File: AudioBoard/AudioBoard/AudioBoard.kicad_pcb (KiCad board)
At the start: 4 copper layers, 250 x 160 mm, 211 parts, among them U5 TL072, U6 TL072, U7 TL072, U8 TL072, U9 TL072

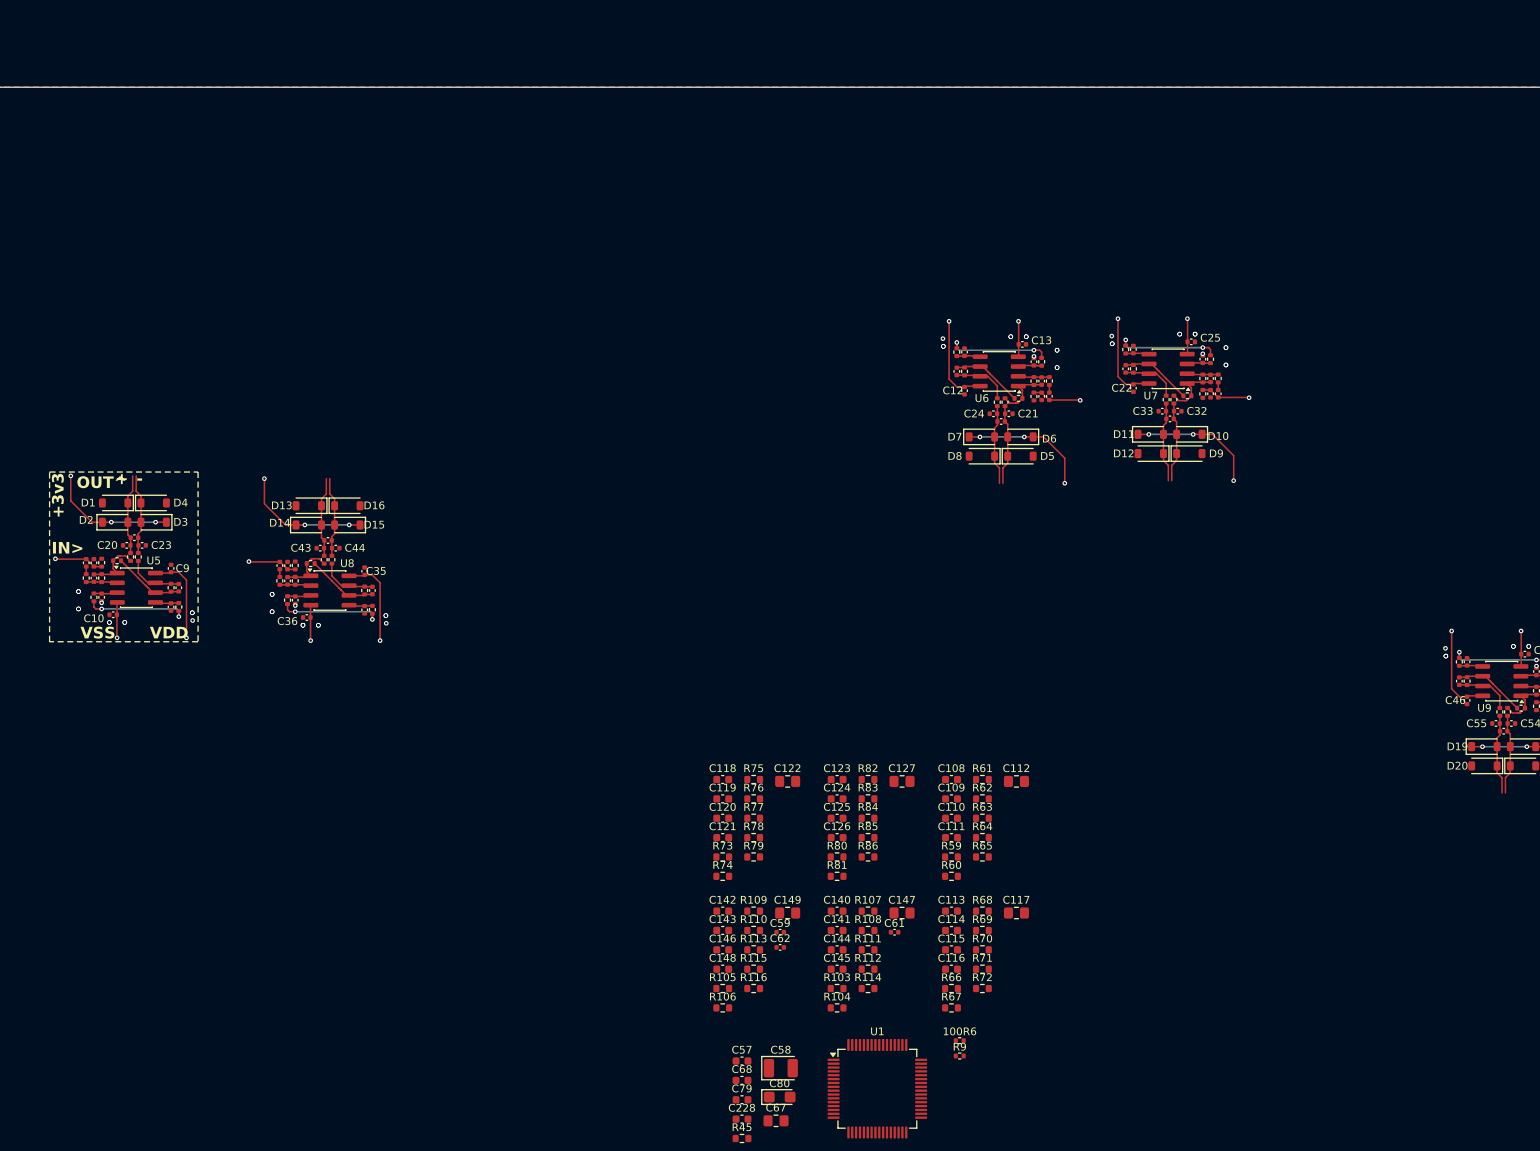
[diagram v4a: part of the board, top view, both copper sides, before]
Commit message: added jack IO, headphone amp cirucit
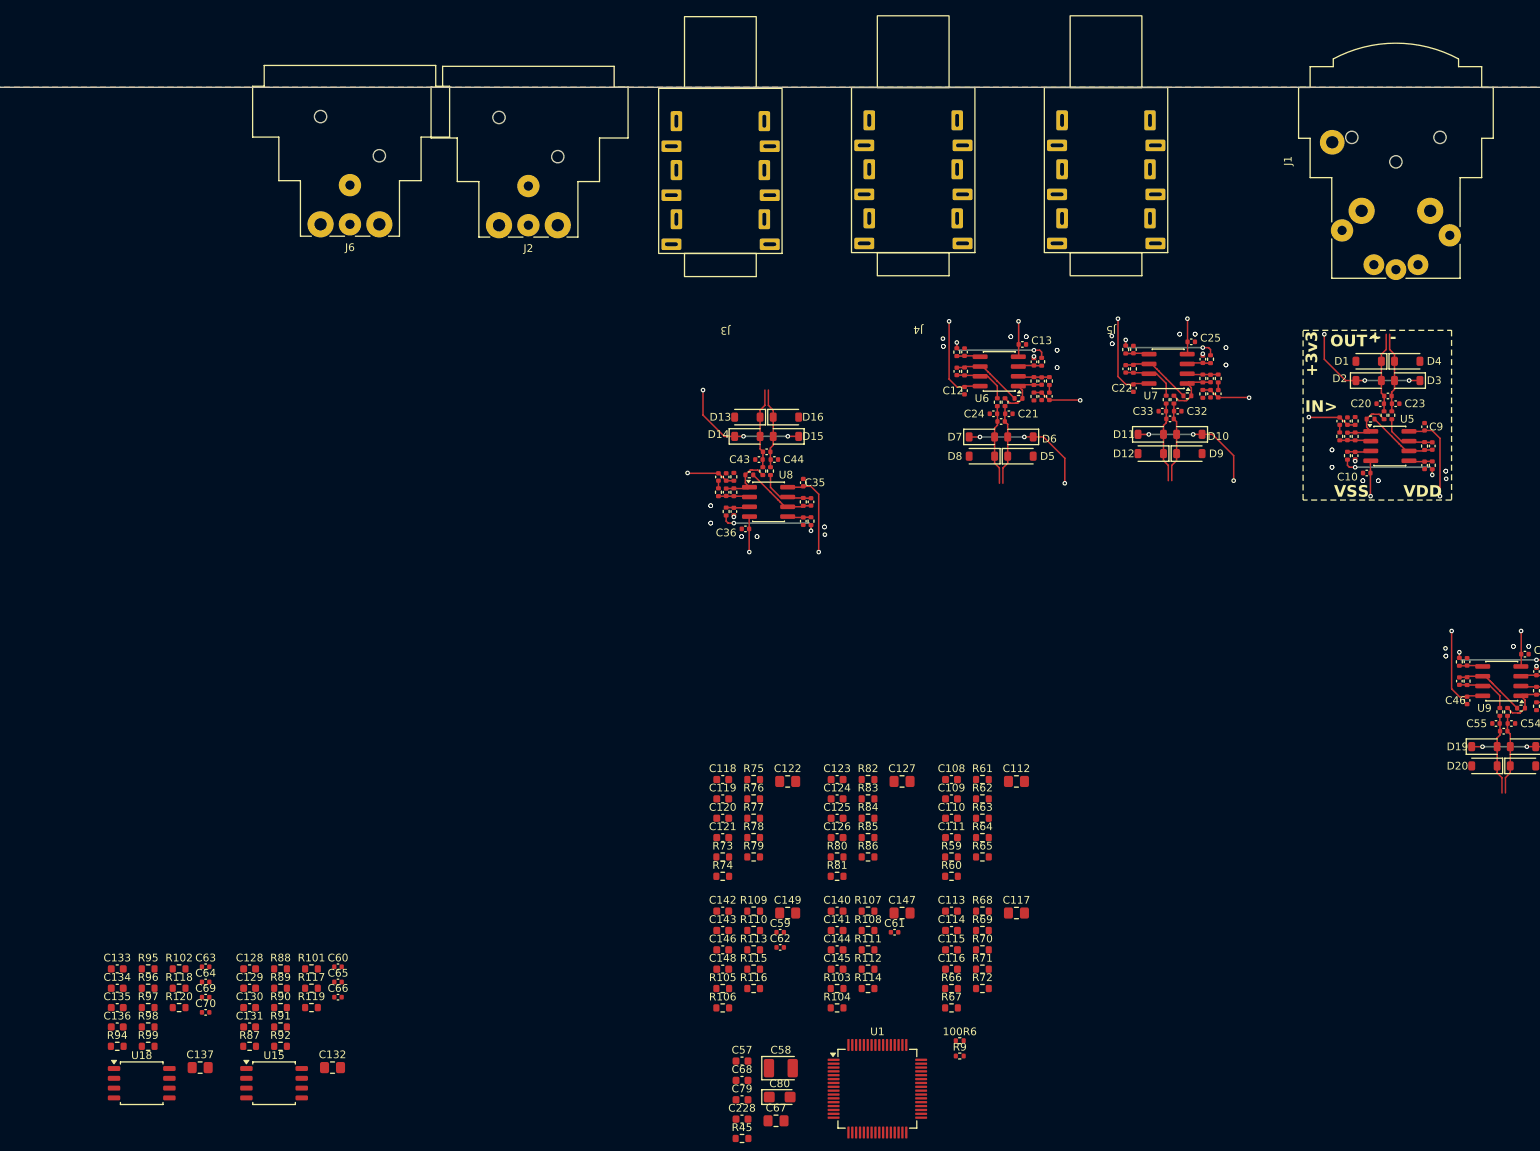
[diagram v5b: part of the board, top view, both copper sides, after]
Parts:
- added C128: 470pF, Capacitor_SMD:C_0603_1608Metric, F.Cu at (116.7, 174.3)
- added C129: 470pF, Capacitor_SMD:C_0603_1608Metric, F.Cu at (116.7, 176.8)
- added C130: 100pF, Capacitor_SMD:C_0603_1608Metric, F.Cu at (116.7, 179.3)
- added C131: 100pF, Capacitor_SMD:C_0603_1608Metric, F.Cu at (116.7, 181.8)
- added C132: 2.2uF, Capacitor_SMD:C_0805_2012Metric_Pad1.18x1.45mm_HandSolder, F.Cu at (127.4, 187.1)
- added C133: 470pF, Capacitor_SMD:C_0603_1608Metric, F.Cu at (99.5, 174.3)
- added C134: 470pF, Capacitor_SMD:C_0603_1608Metric, F.Cu at (99.5, 176.8)
- added C135: 100pF, Capacitor_SMD:C_0603_1608Metric, F.Cu at (99.5, 179.3)
- added C136: 100pF, Capacitor_SMD:C_0603_1608Metric, F.Cu at (99.5, 181.8)
- added C137: 2.2uF, Capacitor_SMD:C_0805_2012Metric_Pad1.18x1.45mm_HandSolder, F.Cu at (110.3, 187.1)
- added C60: 100n, Capacitor_SMD:C_0402_1005Metric, F.Cu at (128.1, 174.0)
- added C63: 100n, Capacitor_SMD:C_0402_1005Metric, F.Cu at (111.0, 174.0)
- added C64: 100n, Capacitor_SMD:C_0402_1005Metric, F.Cu at (111.0, 176.0)
- added C65: 100n, Capacitor_SMD:C_0402_1005Metric, F.Cu at (128.1, 176.0)
- added C66: 100n, Capacitor_SMD:C_0402_1005Metric, F.Cu at (128.1, 178.0)
- added C69: 100n, Capacitor_SMD:C_0402_1005Metric, F.Cu at (111.0, 178.0)
- added C70: 100n, Capacitor_SMD:C_0402_1005Metric, F.Cu at (111.0, 179.9)
- added J1: IN, Connector_Audio:Jack_XLR-6.35mm_Neutrik_NCJ6FA-H_Horizontal, F.Cu at (258.3, 78.6)
- added J2: XLR_L, Connector_Audio:Jack_XLR_Neutrik_NC3MAH_Horizontal, F.Cu at (156.6, 77.9)
- added J3: FX_RETURN, haoyu:HAOYU_PJ-625, F.Cu at (182.4, 84.5)
- added J4: FX_SEND, haoyu:HAOYU_PJ-625, F.Cu at (207.4, 84.4)
- added J5: INS_OUT, haoyu:HAOYU_PJ-625, F.Cu at (232.3, 84.4)
- added J6: XLR_R, Connector_Audio:Jack_XLR_Neutrik_NC3MAH_Horizontal, F.Cu at (133.5, 77.8)
- added R101: 40k, Resistor_SMD:R_0603_1608Metric, F.Cu at (124.7, 174.3)
- added R102: 40k, Resistor_SMD:R_0603_1608Metric, F.Cu at (107.5, 174.3)
- added R117: 1R, Resistor_SMD:R_0603_1608Metric, F.Cu at (124.7, 176.8)
- added R118: 1R, Resistor_SMD:R_0603_1608Metric, F.Cu at (107.5, 176.8)
- added R119: 1R, Resistor_SMD:R_0603_1608Metric, F.Cu at (124.7, 179.3)
- added R120: 1R, Resistor_SMD:R_0603_1608Metric, F.Cu at (107.5, 179.3)
- added R87: 3k, Resistor_SMD:R_0603_1608Metric, F.Cu at (116.7, 184.3)
- added R88: 3k, Resistor_SMD:R_0603_1608Metric, F.Cu at (120.7, 174.3)
- added R89: 3k, Resistor_SMD:R_0603_1608Metric, F.Cu at (120.7, 176.8)
- added R90: 3k, Resistor_SMD:R_0603_1608Metric, F.Cu at (120.7, 179.3)
- added R91: 3k, Resistor_SMD:R_0603_1608Metric, F.Cu at (120.7, 181.8)
- added R92: 3k, Resistor_SMD:R_0603_1608Metric, F.Cu at (120.7, 184.3)
- added R94: 3k, Resistor_SMD:R_0603_1608Metric, F.Cu at (99.5, 184.3)
- added R95: 3k, Resistor_SMD:R_0603_1608Metric, F.Cu at (103.5, 174.3)
- added R96: 3k, Resistor_SMD:R_0603_1608Metric, F.Cu at (103.5, 176.8)
- added R97: 3k, Resistor_SMD:R_0603_1608Metric, F.Cu at (103.5, 179.3)
- added R98: 3k, Resistor_SMD:R_0603_1608Metric, F.Cu at (103.5, 181.8)
- added R99: 3k, Resistor_SMD:R_0603_1608Metric, F.Cu at (103.5, 184.3)
- added U15: NJM4556A, Package_SO:SOIC-8_5.3x5.3mm_P1.27mm, F.Cu at (119.8, 189.1)
- added U18: NJM4556A, Package_SO:SOIC-8_5.3x5.3mm_P1.27mm, F.Cu at (102.7, 189.1)
- C55: value 1n -> 100n
- moved 100R1 163.6 mm to (270.0, 109.0)
- moved C10 163.6 mm to (261.5, 110.0)
- moved C11 163.6 mm to (259.0, 105.3)
- moved C14 163.6 mm to (270.0, 106.5)
- moved C17 163.6 mm to (269.0, 109.0)
- moved C2 163.6 mm to (259.0, 103.3)
- moved C20 163.6 mm to (263.2, 101.0)
- moved C23 163.6 mm to (265.2, 101.0)
- moved C26 163.6 mm to (264.2, 100.0)
- moved C5 163.6 mm to (258.0, 103.3)
- moved C8 163.6 mm to (260.0, 107.8)
- moved C9 163.6 mm to (269.0, 104.0)
- moved D1 163.6 mm to (261.8, 98.0)
- moved D2 163.6 mm to (261.8, 95.5)
- moved D3 163.6 mm to (266.8, 98.0)
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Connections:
- net /MIC_preamp/IN_N renamed /Audio_IO_conn/xlr_in_n
- net /MIC_preamp/IN_P renamed /Audio_IO_conn/xlr_in_p
- C55 pad 1: /Instrument_Input5/OUT_N -> /HeadphoneAmplifier/VDD
- R4 pad 1: /Instrument_Input/IN -> /Audio_IO_conn/ins_in
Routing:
- net (no net): track 26.1 -> 14.1 mm, vias 3 -> 2
- net VDD: track 48.0 -> 60.0 mm, vias 4 -> 5

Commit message: added connectors to pcb
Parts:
- added J7: Barrel_Jack, Connector_BarrelJack:BarrelJack_Wuerth_6941xx301002, F.Cu at (59.5, 74.0)
- added J8: NMJ6HFD2, Connector_Audio:Jack_6.35mm_Neutrik_NMJ6HFD2_Horizontal, F.Cu at (89.3, 76.8)
- added J9: NMJ6HFD2, Connector_Audio:Jack_6.35mm_Neutrik_NMJ6HFD2_Horizontal, F.Cu at (282.0, 77.0)
- added SW2: SW_SPDT_321, haoyu:SS-12D28G7, F.Cu at (70.0, 84.6)
- added SW3: PWR_SW, haoyu:SS-12D28G7, F.Cu at (111.0, 84.6)

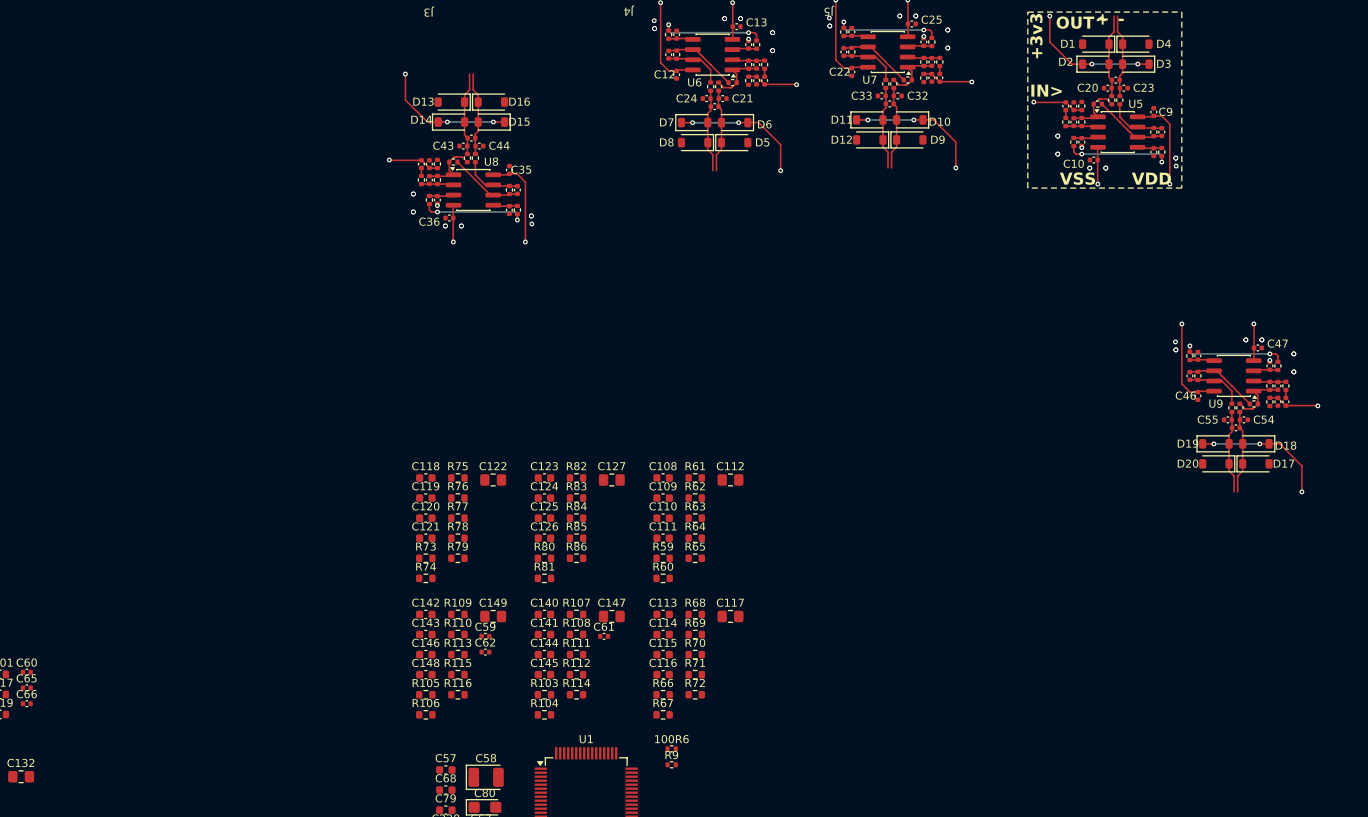
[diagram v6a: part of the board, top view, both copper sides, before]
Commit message: added lcscpart to components and assigned footprints
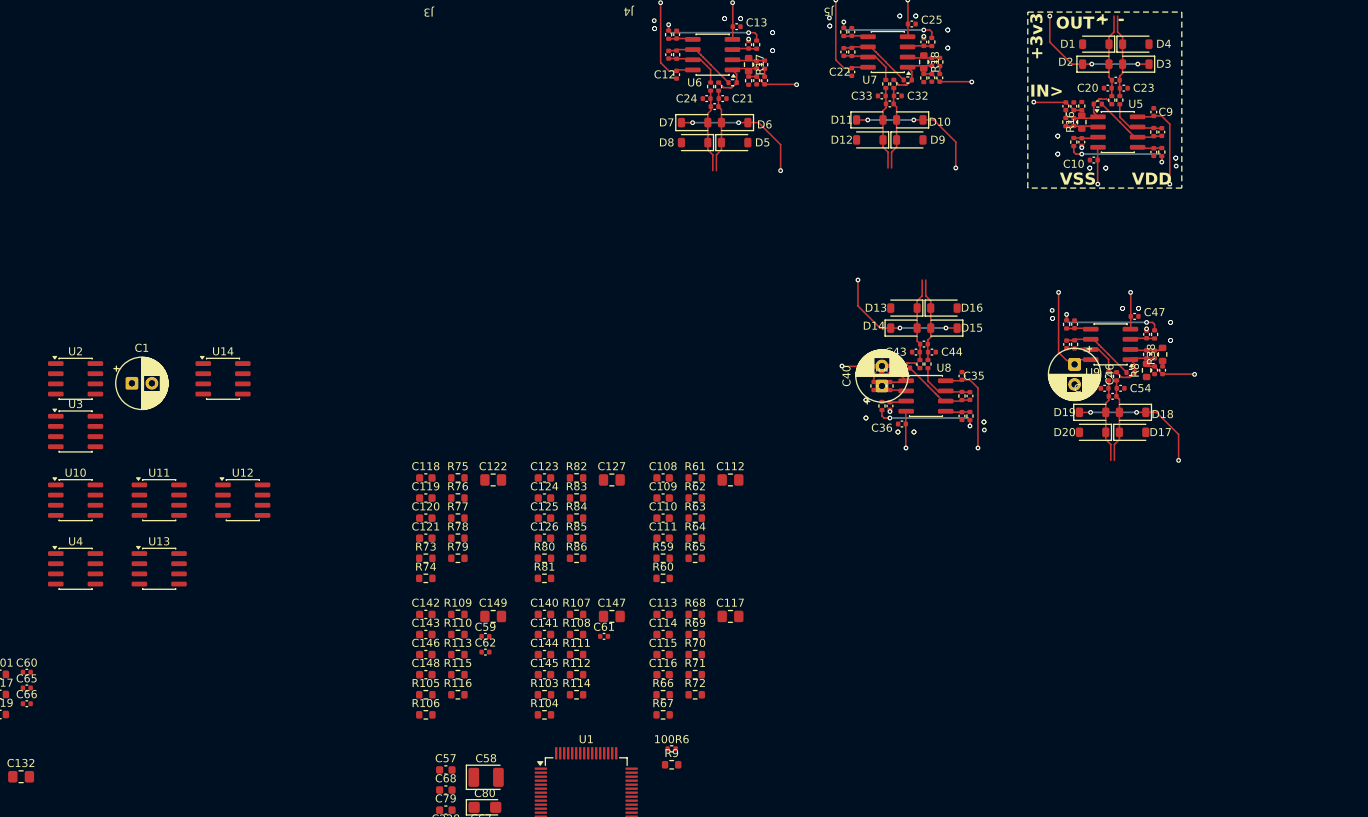
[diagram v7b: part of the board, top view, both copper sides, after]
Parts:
- added C1: 47u, Capacitor_THT:CP_Radial_D6.3mm_P2.50mm, F.Cu at (141.3, 137.9)
- added U10: TL072, Package_SO:SOIC-8_3.9x4.9mm_P1.27mm, F.Cu at (134.2, 152.5)
- added U11: TL072, Package_SO:SOIC-8_3.9x4.9mm_P1.27mm, F.Cu at (144.7, 152.5)
- added U12: TL072, Package_SO:SOIC-8_3.9x4.9mm_P1.27mm, F.Cu at (155.1, 152.5)
- added U13: TL072, Package_SO:SOIC-8_3.9x4.9mm_P1.27mm, F.Cu at (144.7, 161.1)
- added U14: TL072, Package_SO:SOIC-8_3.9x4.9mm_P1.27mm, F.Cu at (152.7, 137.4)
- added U2: NE5532, Package_SO:SOIC-8_3.9x4.9mm_P1.27mm, F.Cu at (134.2, 137.4)
- added U3: NE5532, Package_SO:SOIC-8_3.9x4.9mm_P1.27mm, F.Cu at (134.2, 143.9)
- added U4: TL072, Package_SO:SOIC-8_3.9x4.9mm_P1.27mm, F.Cu at (134.2, 161.1)
- C40, C46: footprint Capacitor_SMD:C_0402_1005Metric -> Capacitor_THT:CP_Radial_D6.3mm_P2.50mm
- R16, R17, R18, R38, R8, R9: footprint Resistor_SMD:R_0402_1005Metric -> Resistor_SMD:R_0603_1608Metric
- moved C43 62.2 mm to (239.3, 134.0)
- moved C44 62.2 mm to (241.3, 134.0)
- moved C45 62.2 mm to (240.3, 133.0)
- moved D13 62.2 mm to (237.8, 131.0)
- moved D14 62.2 mm to (237.8, 128.5)
- moved D15 62.2 mm to (242.8, 131.0)
- moved D16 62.2 mm to (242.8, 128.5)
- moved R36 62.2 mm to (240.8, 135.5)
- moved R37 62.2 mm to (239.8, 135.5)
- moved 100R4 62.2 mm to (246.0, 142.0)
- moved C35 62.2 mm to (245.0, 137.0)
- moved C36 62.2 mm to (237.5, 143.0)
- moved C37 62.2 mm to (235.0, 136.3)
- moved C38 62.2 mm to (234.0, 136.3)
- moved C39 62.2 mm to (236.0, 140.8)
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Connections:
- R38 pad 1: Net-(SW1-B) -> +48V
